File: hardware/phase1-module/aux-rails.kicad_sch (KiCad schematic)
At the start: 0 parts

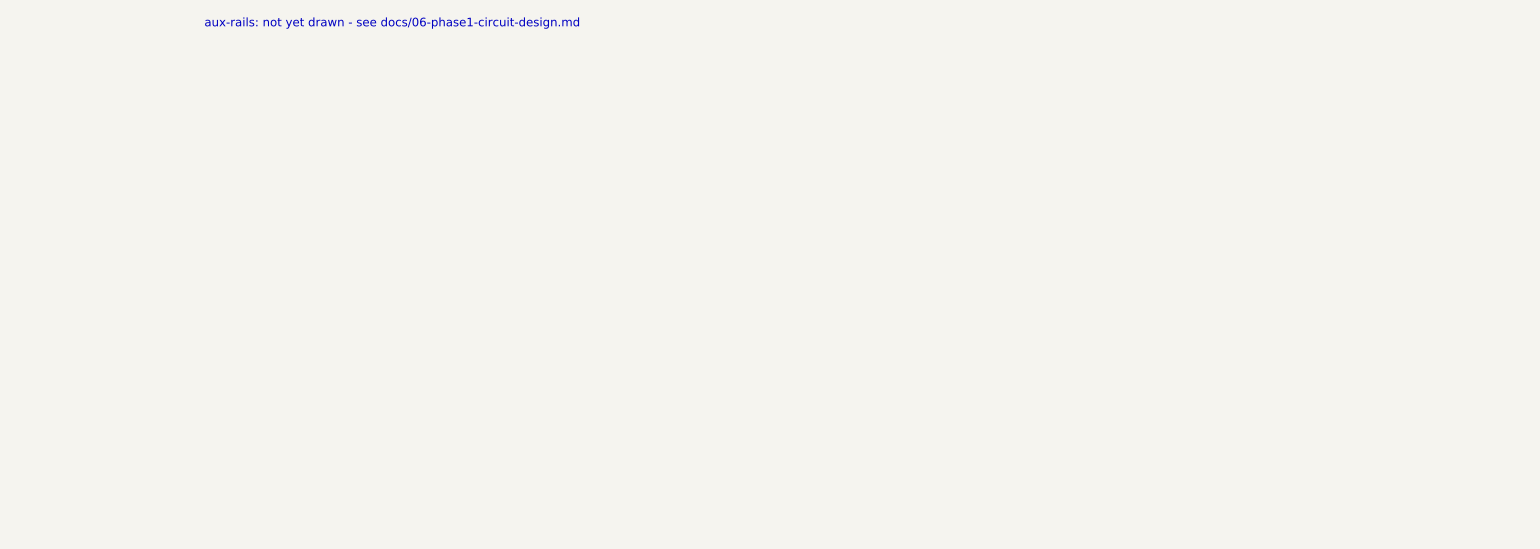
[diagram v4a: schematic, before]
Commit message: Complete Phase-1 schematic: all six remaining sheets, netlist-verified
- power-stage: LM5145 @350kHz (RT 28.7K per ds eq.3), RDS(on) valley
  ILIM 365R->SW, UVLO divider, EN kill chain (NOT(HW_EN) OR PS_OFF via
  Q5/Q6 + diode-OR), Type-III comp starting values, SYNCIN as DEM/FPWM
- sensing: 2m shunt, INA240A3 -> CC loop, INA228 telemetry, /8 divider,
  NT1 single AGND-PGND tie
- disconnect: back-to-back FETs + LTC7004, INP = OUT_REQ AND NOT(kill)
  AND NOT(OVP); TLV7011 + Q9 trips at 22.25V
- aux-rails: LMR36015 (5.016V) -> NCP1117 3V3
- mcu-can: STM32G431CBT6 fully pinned; I2C moved to I2C2/PA8-PA9 (PB8
  is the BOOT0 strap - pullup there would boot the ROM loader), BOOT0
  strapped low, OUT_REQ on PB14 (PB4 NJTRST reset pull-up), 8MHz
  crystal for CAN, TCAN1042 (VCC 5V, VIO 3V3)
- io: fused input + SMBJ33A TVS, output, backplane header, fan switch
  (1N4148W flyback orientation corrected: pin 1 = cathode)
- checker: duplicate-ref detection + global/local split-net detection;
  caught duplicate C62 and the LMR36015 FB-pin placement collision

Co-Authored-By: Claude Fable 5 <noreply@anthropic.com>
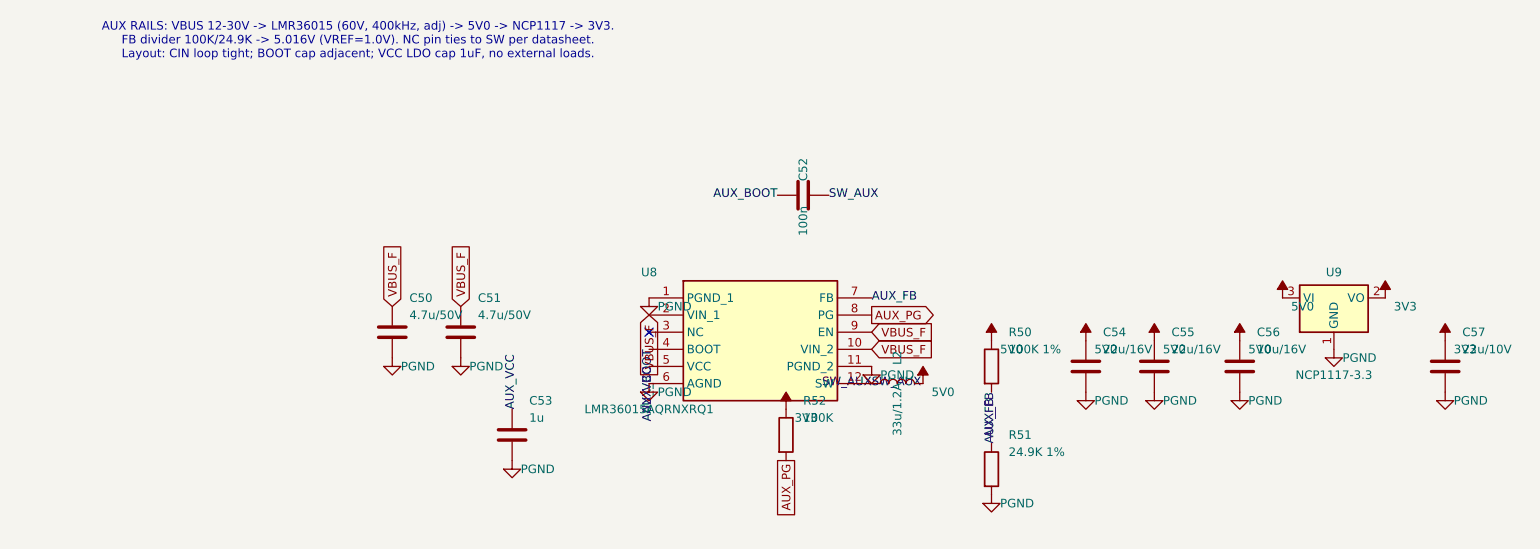
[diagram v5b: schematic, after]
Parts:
- added C50, C51: 4.7u/50V, Capacitor_SMD:C_1210_3225Metric, symbol Device:C
- added C52: 100n, Capacitor_SMD:C_0402_1005Metric, symbol Device:C
- added C53: 1u, Capacitor_SMD:C_0402_1005Metric, symbol Device:C
- added C54, C55: 22u/16V, Capacitor_SMD:C_1210_3225Metric, symbol Device:C
- added C56: 10u/16V, Capacitor_SMD:C_1210_3225Metric, symbol Device:C
- added C57: 22u/10V, Capacitor_SMD:C_1210_3225Metric, symbol Device:C
- added L2: 33u/1.2A, Inductor_SMD:L_1210_3225Metric, symbol Device:L
- added R50: 100K 1%, Resistor_SMD:R_0402_1005Metric, symbol Device:R
- added R51: 24.9K 1%, Resistor_SMD:R_0402_1005Metric, symbol Device:R
- added R52: 100K, Resistor_SMD:R_0402_1005Metric, symbol Device:R
- added U8: LMR36015AQRNXRQ1, labbench:LMR36015_RNX_VQFN-HR-12, symbol labbench:LMR36015AQRNXRQ1
- added U9: NCP1117-3.3, Package_TO_SOT_SMD:SOT-223-3_TabPin2, symbol Regulator_Linear:NCP1117-3.3_SOT223
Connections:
- new net 3V3: C57.1, R52.1, U9.2 (VO)
- new net 5V0: C54.1, C55.1, C56.1, L2.2, R50.1, U9.3 (VI)
- new net AUX_BOOT: C52.1, U8.4 (BOOT)
- new net AUX_FB: R50.2, R51.1, U8.7 (FB)
- new net AUX_PG: R52.2, U8.8 (PG)
- new net AUX_VCC: C53.1, U8.5 (VCC)
- new net PGND: C50.2, C51.2, C53.2, C54.2, C55.2, C56.2, C57.2, R51.2, U8.1 (PGND_1), U8.11 (PGND_2), U8.6 (AGND), U9.1 (GND)
- new net SW_AUX: C52.2, L2.1, U8.12 (SW)
- new net VBUS_F: C50.1, C51.1, U8.10 (VIN_2), U8.2 (VIN_1), U8.9 (EN)
- no-connect marks 0 -> 1
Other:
- note added: "AUX RAILS: VBUS 12-30V -> LMR36015 (60V, 400kHz, adj) -> 5V0 -> NCP1117 -> 3V3. FB divider 100K/24.9K -> 5.016V (VREF=1.0V). NC pin ties to SW per datasheet. Layout: CIN loop tight; BOOT cap adjacent; VCC LDO cap 1uF, no external loads."
- note removed: "aux-rails: not yet drawn - see docs/06-phase1-circuit-design.md"

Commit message: Footprint pass: labbench.pretty library, all 137 components verified
- build_fplib.py: merges vetted vendor footprints (LM5145 RGY0020B,
  LMR36015 RNX, DAC80502 WSON-10 no-EP) and generates PowerFET_SON5x6_GDS
  from the TI Q5A land pattern (CSD18563Q5A SLPS444C) with pads renumbered
  1=G/2=D/3=S to match the generic NMOS symbol; writes fp-lib-table.
- check_footprints.py: every component must have a resolvable footprint and
  every netted pin a matching pad (caught a wrong official VSSOP-8 name).
- gen_phase1.py: passives 0402->0603 (hand assembly); DAC80502 vendor fp
  (DRX has no exposed pad); L1 = Coilcraft XAL1350-103ME on official fp;
  net-tie fp; crystal -> Crystal_GND24 with grounded shield pads; bulk cap
  banks expanded to one component per physical cap (C75-C81); R27 preload
  1W -> 2512.
- PARTS-TO-DOWNLOAD.md section D: new orderables for the footprint pass.

check_netlist + check_footprints: all OK (137 components).

Co-Authored-By: Claude Fable 5 <noreply@anthropic.com>
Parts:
- C52, C53: footprint Capacitor_SMD:C_0402_1005Metric -> Capacitor_SMD:C_0603_1608Metric
- R50, R51, R52: footprint Resistor_SMD:R_0402_1005Metric -> Resistor_SMD:R_0603_1608Metric
